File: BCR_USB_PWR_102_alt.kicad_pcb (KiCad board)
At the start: 2 copper layers, 32.2 x 17 mm, 2 parts, among them CN1 DB9_Female, CN2 UE27AC54100

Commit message: clean up junk files
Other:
- board text added: "HAZARD!!!"
- board text added: "SHORTING"
- board text removed: "SHORTING HAZARD !!!"
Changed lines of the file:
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@@
   (general
     (thickness 1.6)
-    (drawings 17)
+    (drawings 21)
     (tracks 4)
     (zones 0)
@@
     )
   )
-  (gr_text "SHORTING HAZARD !!!" (at 121.65 99.058) (layer F.SilkS)
+  (gr_text HAZARD!!! (at 122.85 100.633) (layer F.SilkS)
     (effects (font (size 0.8 0.8) (thickness 0.08)))
   )
+  (gr_line (start 122.85 96.083) (end 122.85 98.858) (layer F.SilkS) (width 0.1016))
+  (gr_line (start 122.15 95.733) (end 122.85 96.083) (layer F.SilkS) (width 0.1016))
+  (gr_line (start 121.9 96.258) (end 122.375 95.258) (layer F.SilkS) (width 0.1016))
+  (gr_text SHORTING (at 122.85 99.633) (layer F.SilkS)
+    (effects (font (size 0.8 0.8) (thickness 0.08)))
+  )

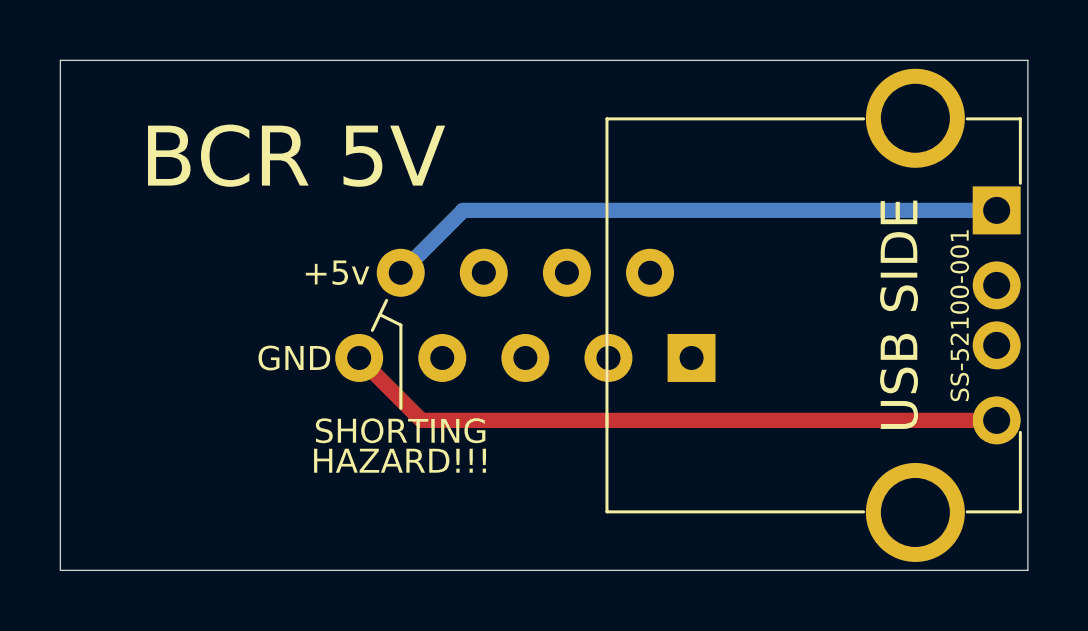
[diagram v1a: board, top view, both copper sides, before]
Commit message: rename NEC to up_long, and a short up version that covers up the shorting hazard
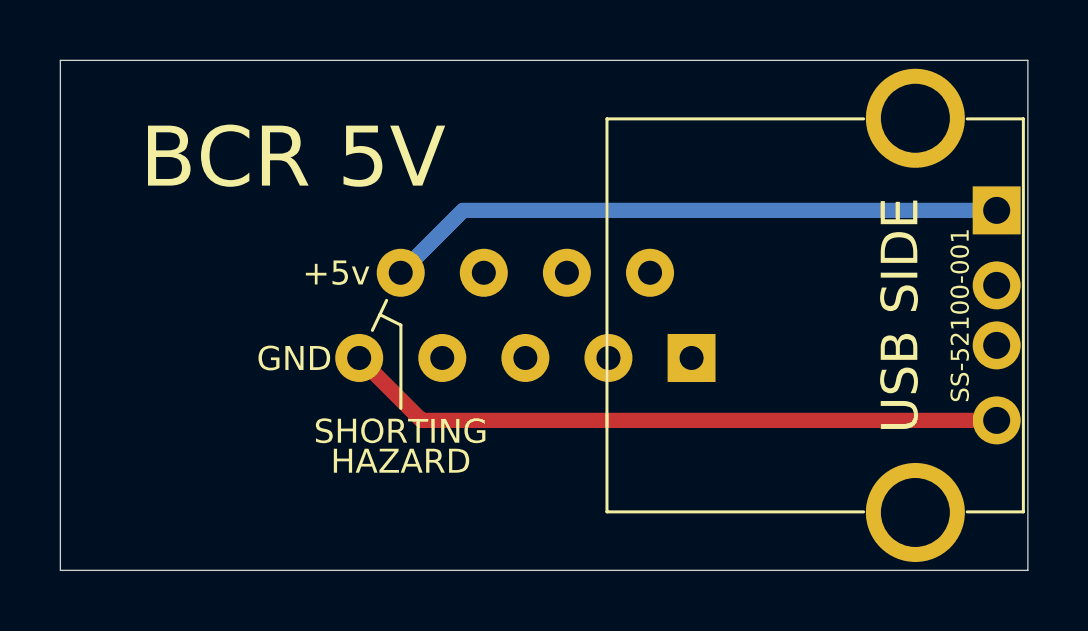
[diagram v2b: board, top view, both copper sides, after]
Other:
- board text added: "HAZARD"
- board text removed: "HAZARD!!!"
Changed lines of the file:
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@@
     (add_net "Net-(CN2-PadSH)")
+  )
+  (module 0_LOCAL:USB_A_Female_UE27AC54100 (layer F.Cu)
+    (at 140 95.758 270)
+    (fp_text reference CN2 (at 0 -0.889 270 unlocked) (layer F.SilkS) hide
+      (effects (font (size 1 1) (thickness 0.15)))
+    )
+    (fp_text value UE27AC54100 (at 0 11.35 270) (layer F.Fab)
+      (effects (font (size 1 1) (thickness 0.15)))
+    )
+    (fp_line (start -6.55 -3.6) (end 6.55 -3.6) (layer F.SilkS) (width 0.1))
+    (fp_line (start 6.55 1.725) (end 6.55 10.28) (layer F.SilkS) (width 0.1))
+    (fp_line (start -6.55 1.725) (end -6.55 10.28) (layer F.SilkS) (width 0.1))
+    (fp_line (start -6.55 -3.6) (end -6.55 -1.725) (layer F.SilkS) (width 0.1))
+    (fp_line (start -6.55 -3.6) (end 6.55 -3.6) (layer F.Fab) (width 0.1))
+    (fp_line (start 6.55 -3.6) (end 6.55 10.28) (layer F.Fab) (width 0.1))
+    (fp_line (start -6.55 -3.6) (end -6.55 10.28) (layer F.Fab) (width 0.1))
+    (fp_line (start -6.55 10.28) (end 6.55 10.28) (layer F.Fab) (width 0.1))
+    (fp_line (start 6.55 -3.6) (end 6.55 -1.725) (layer F.SilkS) (width 0.1))
+    (fp_line (start 6.55 10.28) (end -6.55 10.28) (layer F.SilkS) (width 0.1))
+    (fp_line (start -8.45 -3.94) (end 8.45 -3.94) (layer F.CrtYd) (width 0.05))
+    (fp_line (start 8.45 -3.94) (end 8.45 10.375) (layer F.CrtYd) (width 0.05))
+    (fp_line (start -8.45 -3.94) (end -8.45 10.375) (layer F.CrtYd) (width 0.05))
+    (fp_line (start -8.45 10.375) (end 8.45 10.375) (layer F.CrtYd) (width 0.05))
+    (fp_text user %R (at -0.025 0.975 270) (layer F.Fab)
+      (effects (font (size 1 1) (thickness 0.15)))
+    )
+    (pad 4 thru_hole circle (at 3.5 -2.71 270) (size 1.6 1.6) (drill 0.9) (layers *.Cu *.Mask)
+      (net 2 /GND))
+    (pad 3 thru_hole circle (at 1 -2.71 270) (size 1.6 1.6) (drill 0.9) (layers *.Cu *.Mask))
+    (pad 2 thru_hole circle (at -1 -2.71 270) (size 1.6 1.6) (drill 0.9) (layers *.Cu *.Mask))
+    (pad 1 thru_hole rect (at -3.5 -2.71 270) (size 1.6 1.6) (drill 0.9) (layers *.Cu *.Mask)
+      (net 1 /+5V))
+    (pad SH thru_hole circle (at 6.57 0 270) (size 3.3 3.3) (drill 2.3) (layers *.Cu *.Mask)
+      (net 3 "Net-(CN2-PadSH)"))
+    (pad SH thru_hole circle (at -6.57 0 270) (size 3.3 3.3) (drill 2.3) (layers *.Cu *.Mask)
+      (net 3 "Net-(CN2-PadSH)"))
+    (model ${KIPRJMOD}/3dmodels/USB-A_female_horiz_thru.step
+      (offset (xyz 0 3.5 6.9))
+      (scale (xyz 1 1 1))
+      (rotate (xyz 0 0 0))
+    )
   )
   (module 0_LOCAL:TE-5207826 (layer B.Cu)
@@
     )
   )
-  (module 0_LOCAL:USB_A_Female_UE27AC54100 (layer F.Cu)
-    (at 140 95.758 270)
-    (fp_text reference CN2 (at 0 -0.889 270 unlocked) (layer F.SilkS) hide
-      (effects (font (size 1 1) (thickness 0.15)))
-    )
-    (fp_text value UE27AC54100 (at 0 11.35 270) (layer F.Fab)
-      (effects (font (size 1 1) (thickness 0.15)))
-    )
-    (fp_line (start -6.55 -3.5) (end -4.4 -3.5) (layer F.SilkS) (width 0.1))
-    (fp_line (start 6.55 1.725) (end 6.55 10.28) (layer F.SilkS) (width 0.1))
-    (fp_line (start -6.55 1.725) (end -6.55 10.28) (layer F.SilkS) (width 0.1))
-    (fp_line (start -6.55 -3.5) (end -6.55 -1.725) (layer F.SilkS) (width 0.1))
-    (fp_line (start -6.55 -3.5) (end 6.55 -3.5) (layer F.Fab) (width 0.1))
-    (fp_line (start 6.55 -3.5) (end 6.55 10.28) (layer F.Fab) (width 0.1))
-    (fp_line (start -6.55 -3.5) (end -6.55 10.28) (layer F.Fab) (width 0.1))
-    (fp_line (start -6.55 10.28) (end 6.55 10.28) (layer F.Fab) (width 0.1))
-    (fp_line (start 3.9 -3.5) (end 6.55 -3.5) (layer F.SilkS) (width 0.1))
-    (fp_line (start 6.55 -3.5) (end 6.55 -1.725) (layer F.SilkS) (width 0.1))
-    (fp_line (start 6.55 10.28) (end -6.55 10.28) (layer F.SilkS) (width 0.1))
-    (fp_line (start -8.45 -3.94) (end 8.45 -3.94) (layer F.CrtYd) (width 0.05))
-    (fp_line (start 8.45 -3.94) (end 8.45 10.375) (layer F.CrtYd) (width 0.05))
-    (fp_line (start -8.45 -3.94) (end -8.45 10.375) (layer F.CrtYd) (width 0.05))
-    (fp_line (start -8.45 10.375) (end 8.45 10.375) (layer F.CrtYd) (width 0.05))
-    (fp_text user %R (at -0.025 0.975 270) (layer F.Fab)
-      (effects (font (size 1 1) (thickness 0.15)))
-    )
-    (pad 4 thru_hole circle (at 3.5 -2.71 270) (size 1.6 1.6) (drill 0.9) (layers *.Cu *.Mask)
-      (net 2 /GND))
-    (pad 3 thru_hole circle (at 1 -2.71 270) (size 1.6 1.6) (drill 0.9) (layers *.Cu *.Mask))
-    (pad 2 thru_hole circle (at -1 -2.71 270) (size 1.6 1.6) (drill 0.9) (layers *.Cu *.Mask))
-    (pad 1 thru_hole rect (at -3.5 -2.71 270) (size 1.6 1.6) (drill 0.9) (layers *.Cu *.Mask)
-      (net 1 /+5V))
-    (pad SH thru_hole circle (at 6.57 0 270) (size 3.3 3.3) (drill 2.3) (layers *.Cu *.Mask)
-      (net 3 "Net-(CN2-PadSH)"))
-    (pad SH thru_hole circle (at -6.57 0 270) (size 3.3 3.3) (drill 2.3) (layers *.Cu *.Mask)
-      (net 3 "Net-(CN2-PadSH)"))
-    (model ${KIPRJMOD}/3dmodels/USB-A_female_horiz_thru.step
-      (offset (xyz 0 3.5 6.9))
-      (scale (xyz 1 1 1))
-      (rotate (xyz 0 0 0))
-    )
-  )
-  (gr_text HAZARD!!! (at 122.85 100.633) (layer F.SilkS)
+  (gr_text HAZARD (at 122.85 100.633) (layer F.SilkS)
     (effects (font (size 0.8 0.8) (thickness 0.08)))
   )

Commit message: Add BCR_Breakout. Rename repo to BCR_Breakout.
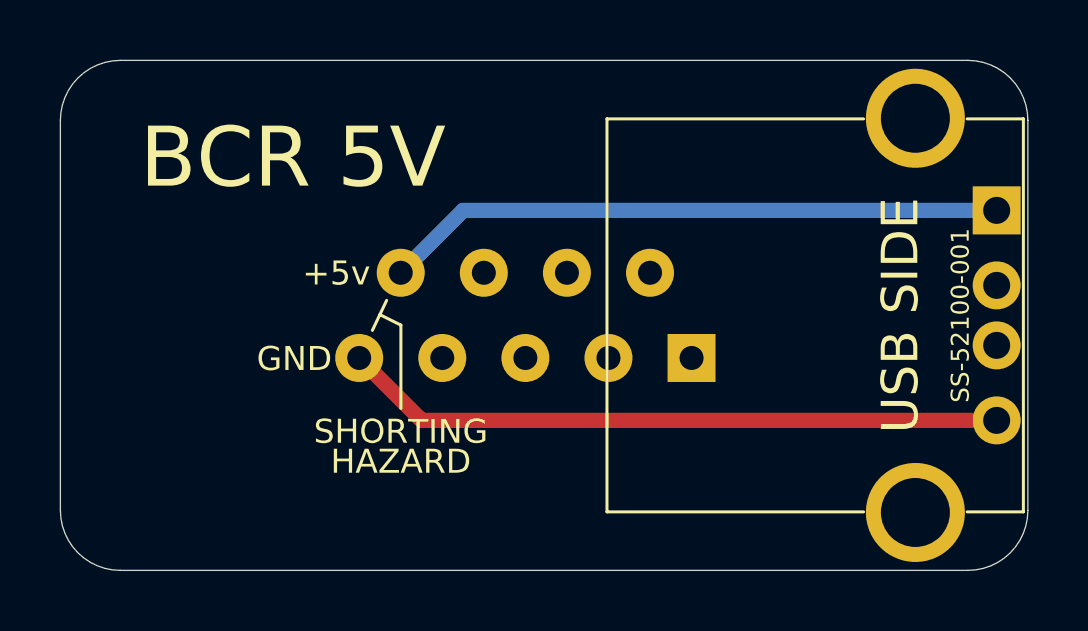
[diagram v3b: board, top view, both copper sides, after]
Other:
- outline, holes or cut-outs redrawn
- board text added: "github.com/bkw777/BCR_Breakout"
- board text removed: "github.com/bkw777/BCR_USB_PWR"
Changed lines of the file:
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@@
   (general
     (thickness 1.6)
-    (drawings 21)
+    (drawings 25)
     (tracks 4)
     (zones 0)
@@
     (uvia_min_size 0.2)
     (uvia_min_drill 0.1)
-    (edge_width 0.05)
+    (edge_width 0.025)
     (segment_width 0.2)
     (pcb_text_width 0.3)
@@
     )
   )
+  (gr_arc (start 113.5 102.258) (end 111.5 102.258) (angle -90) (layer Edge.Cuts) (width 0.025))
+  (gr_arc (start 141.75 102.258) (end 141.75 104.258) (angle -90) (layer Edge.Cuts) (width 0.025))
+  (gr_arc (start 141.75 89.258) (end 143.75 89.258) (angle -90) (layer Edge.Cuts) (width 0.025))
+  (gr_arc (start 113.5 89.258) (end 113.5 87.258) (angle -90) (layer Edge.Cuts) (width 0.025))
   (gr_text HAZARD (at 122.85 100.633) (layer F.SilkS)
     (effects (font (size 0.8 0.8) (thickness 0.08)))
@@
     (effects (font (size 0.6 0.6) (thickness 0.1)))
   )
-  (gr_text github.com/bkw777/BCR_USB_PWR (at 127 103.258) (layer B.SilkS)
+  (gr_text "github.com/bkw777/BCR_Breakout\n" (at 127 103.258) (layer B.SilkS)
     (effects (font (size 0.6 0.6) (thickness 0.1)) (justify mirror))
   )
@@
     (effects (font (size 1.2192 1.2192) (thickness 0.2032)))
   )
-  (gr_line (start 111.5 87.258) (end 111.5 104.258) (layer Edge.Cuts) (width 0.0254))
-  (gr_line (start 143.75 87.258) (end 111.5 87.258) (layer Edge.Cuts) (width 0.0254))
-  (gr_line (start 143.75 104.258) (end 143.75 87.258) (layer Edge.Cuts) (width 0.0254))
-  (gr_line (start 111.5 104.258) (end 143.75 104.258) (layer Edge.Cuts) (width 0.0254))
+  (gr_line (start 111.5 89.258) (end 111.5 102.258) (layer Edge.Cuts) (width 0.0254))
+  (gr_line (start 141.75 87.258) (end 113.5 87.258) (layer Edge.Cuts) (width 0.0254))
+  (gr_line (start 143.75 102.258) (end 143.75 89.258) (layer Edge.Cuts) (width 0.0254))
+  (gr_line (start 113.5 104.258) (end 141.75 104.258) (layer Edge.Cuts) (width 0.0254))
   (segment (start 124.925 92.258) (end 122.845 94.338) (width 0.508) (layer B.Cu) (net 1))
   (segment (start 142.71 92.258) (end 124.925 92.258) (width 0.508) (layer B.Cu) (net 1))

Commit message: change metal db9 to plastic
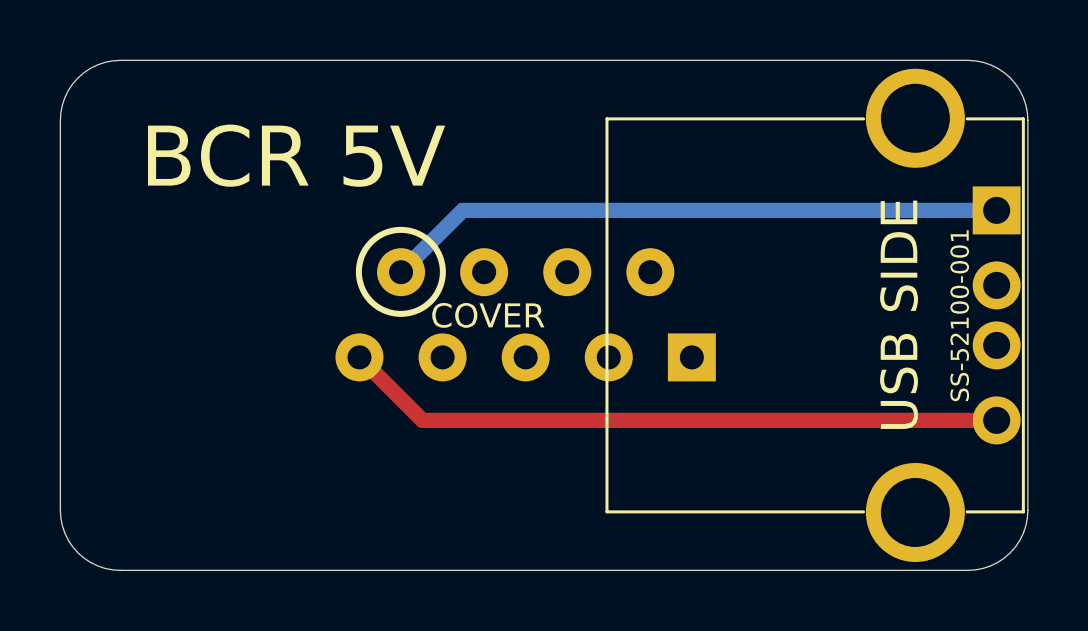
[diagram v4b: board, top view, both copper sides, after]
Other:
- board text added: "COVER"
- board text removed: "+5v"
- board text removed: "GND"
- board text removed: "HAZARD"
- board text removed: "SHORTING"

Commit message: db9 pin 7 is the real GND, not pin 5
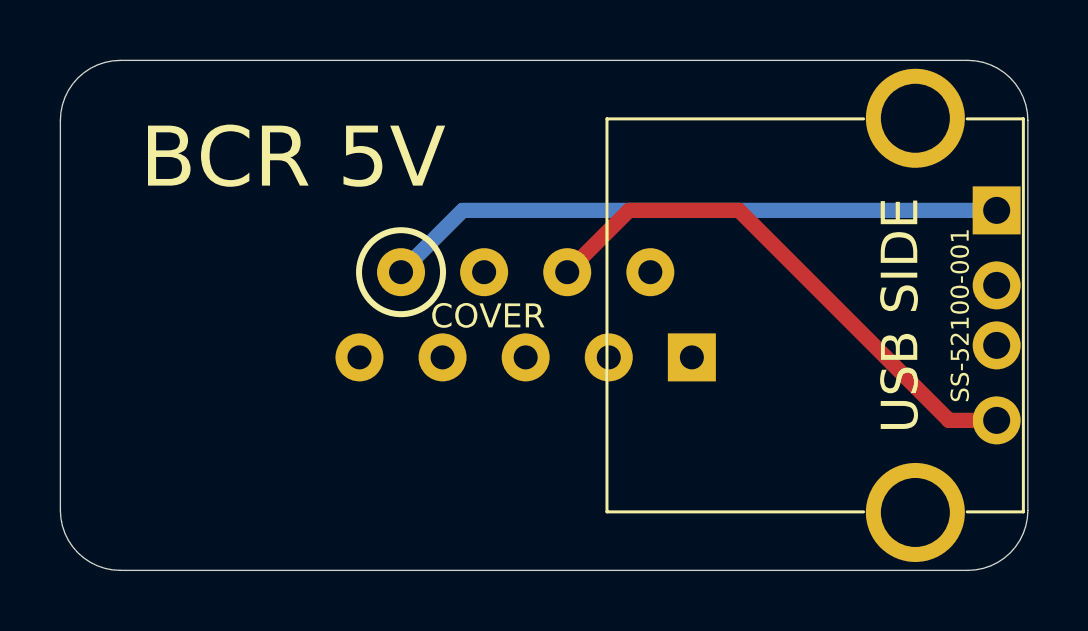
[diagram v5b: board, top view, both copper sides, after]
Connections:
- CN1 pad 5: /GND -> (no net)
- CN1 pad 7: (no net) -> /GND
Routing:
- net /GND: track 22.1 -> 18.1 mm
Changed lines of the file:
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@@
     (thickness 1.6)
     (drawings 24)
-    (tracks 4)
+    (tracks 6)
     (zones 0)
     (modules 2)
@@
     (mod_text_size 1 1)
     (mod_text_width 0.15)
-    (pad_size 1.524 1.524)
-    (pad_drill 0.762)
+    (pad_size 1.6 1.6)
+    (pad_drill 0.8)
     (pad_to_mask_clearance 0)
     (aux_axis_origin 0 0)
@@
       (net 1 /+5V))
     (pad 8 thru_hole circle (at -6.925 -2.84) (size 1.6 1.6) (drill 0.8) (layers *.Cu *.Mask))
-    (pad 7 thru_hole circle (at -4.155 -2.84) (size 1.6 1.6) (drill 0.8) (layers *.Cu *.Mask))
+    (pad 7 thru_hole circle (at -4.155 -2.84) (size 1.6 1.6) (drill 0.8) (layers *.Cu *.Mask)
+      (net 2 /GND))
     (pad 6 thru_hole circle (at -1.385 -2.84) (size 1.6 1.6) (drill 0.8) (layers *.Cu *.Mask))
-    (pad 5 thru_hole circle (at -11.08 0) (size 1.6 1.6) (drill 0.8) (layers *.Cu *.Mask)
-      (net 2 /GND))
+    (pad 5 thru_hole circle (at -11.08 0) (size 1.6 1.6) (drill 0.8) (layers *.Cu *.Mask))
     (pad 4 thru_hole circle (at -8.31 0) (size 1.6 1.6) (drill 0.8) (layers *.Cu *.Mask))
     (pad 3 thru_hole circle (at -5.54 0) (size 1.6 1.6) (drill 0.8) (layers *.Cu *.Mask))
@@
     (effects (font (size 0.8 0.8) (thickness 0.1)))
   )
-  (gr_circle (center 122.85 94.308) (end 124.25 94.308) (layer F.SilkS) (width 0.2))
+  (gr_circle (center 122.855 94.318) (end 124.255 94.318) (layer F.SilkS) (width 0.2))
   (gr_text "TANDY 102" (at 127 89.808) (layer B.SilkS)
     (effects (font (size 1 1) (thickness 0.12)) (justify mirror))
@@
   (segment (start 124.915 92.258) (end 122.855 94.318) (width 0.508) (layer B.Cu) (net 1))
   (segment (start 142.71 92.258) (end 124.915 92.258) (width 0.508) (layer B.Cu) (net 1))
-  (segment (start 123.57 99.258) (end 121.47 97.158) (width 0.508) (layer F.Cu) (net 2))
-  (segment (start 142.71 99.258) (end 123.57 99.258) (width 0.508) (layer F.Cu) (net 2))
+  (segment (start 130.455 92.258) (end 128.395 94.318) (width 0.508) (layer F.Cu) (net 2))
+  (segment (start 134.12 92.258) (end 130.455 92.258) (width 0.508) (layer F.Cu) (net 2))
+  (segment (start 142.71 99.258) (end 141.12 99.258) (width 0.508) (layer F.Cu) (net 2))
+  (segment (start 141.12 99.258) (end 134.12 92.258) (width 0.508) (layer F.Cu) (net 2))
 )
